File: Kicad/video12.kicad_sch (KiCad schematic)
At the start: 18 parts, among them J8001 DE15HD, U8001 THS7316, U8002 TPD7S019

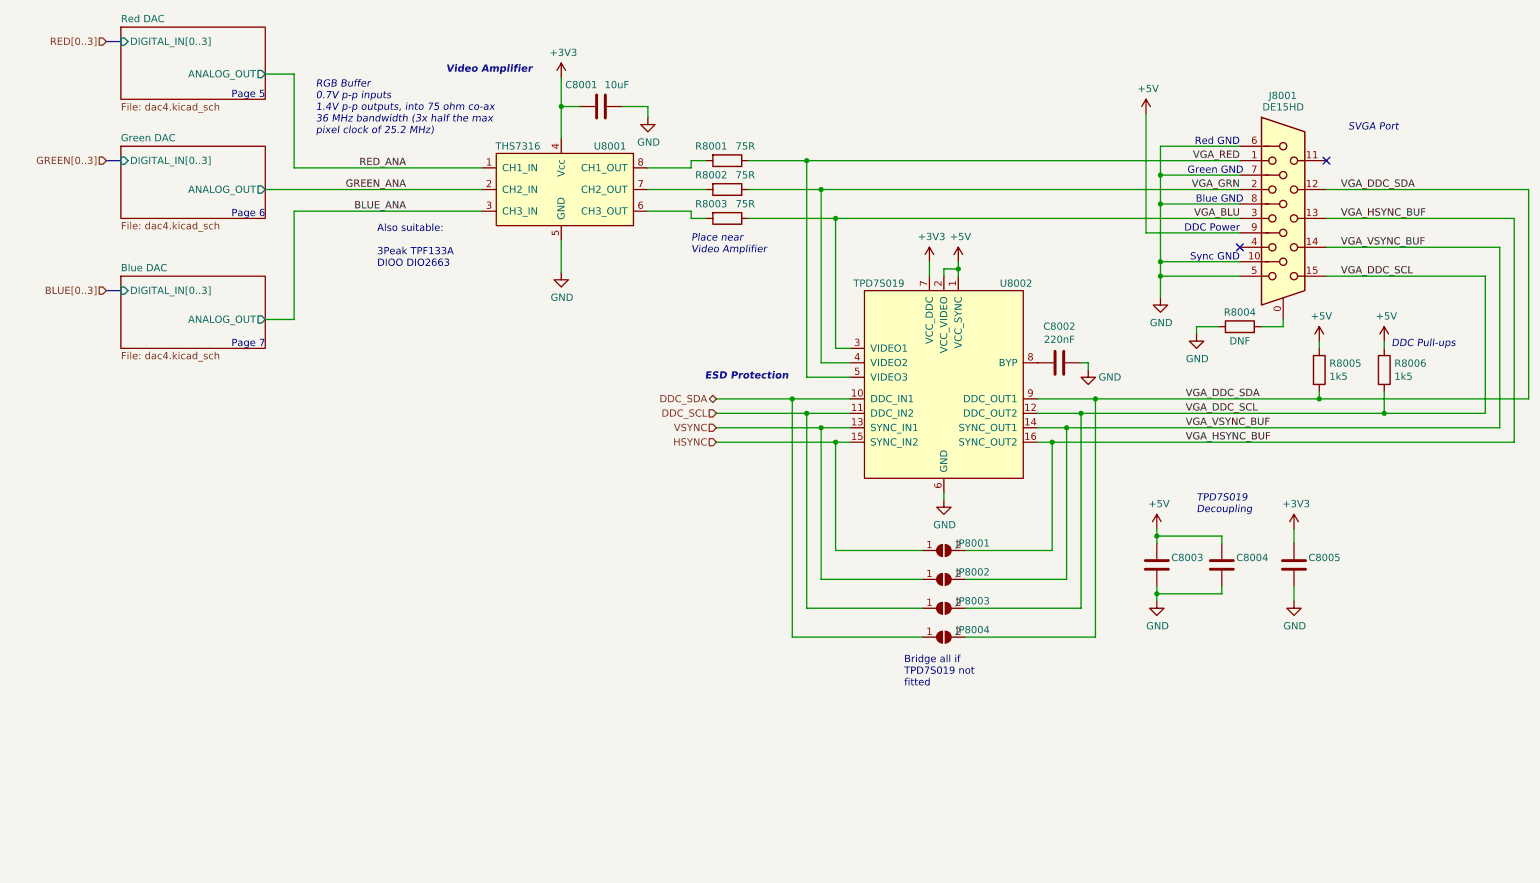
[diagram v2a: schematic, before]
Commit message: Set missing footprints and update PCB
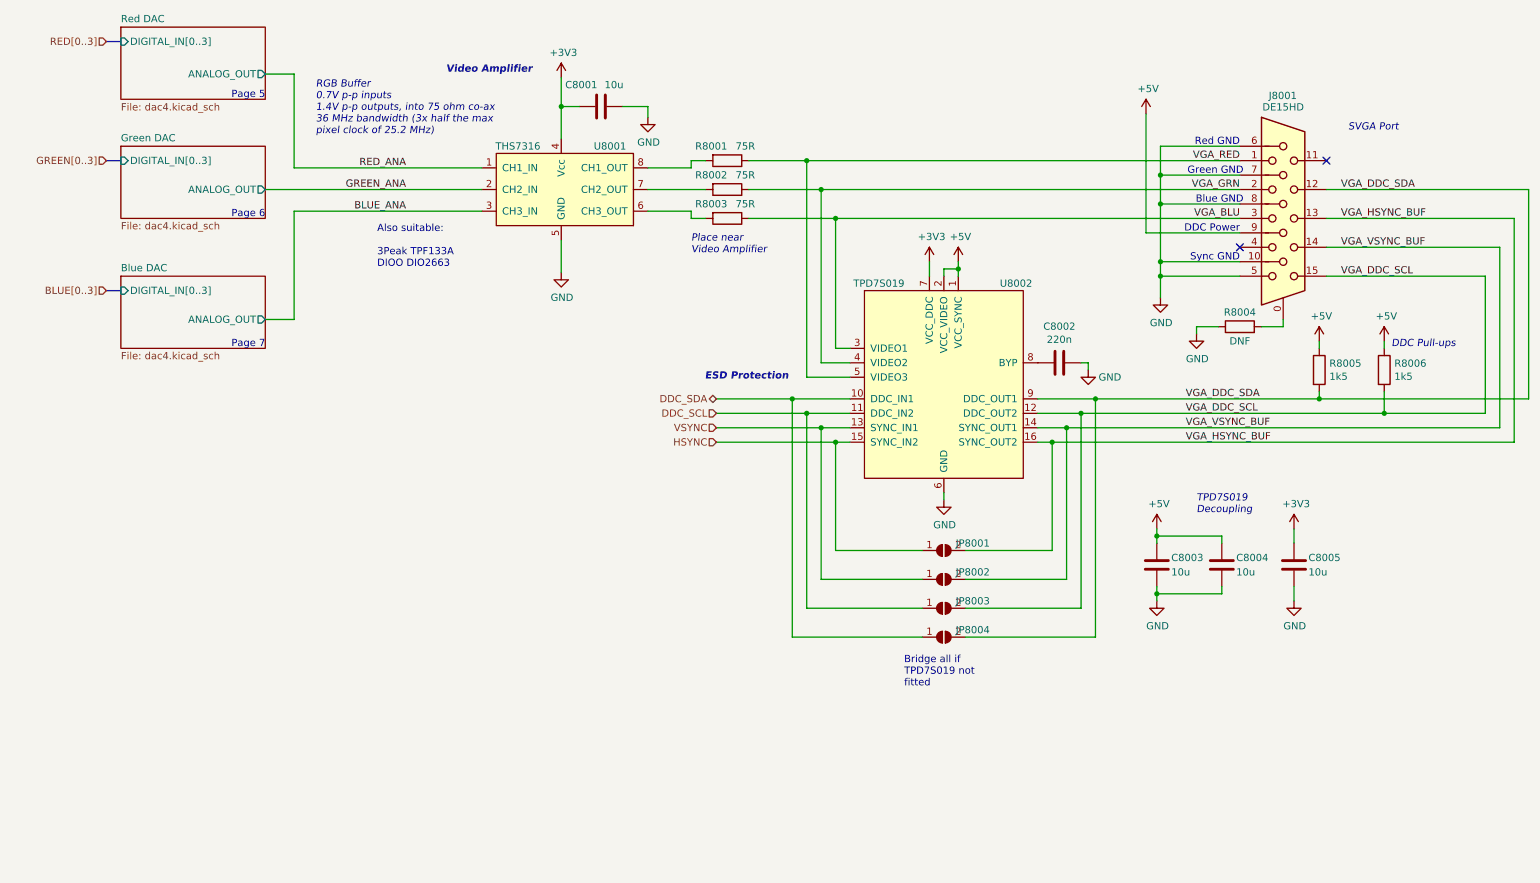
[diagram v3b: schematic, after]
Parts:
- C8001: value 10uF -> 10u; JLCPCB Collection Basic -> (none); LCSC Part# C15850 -> (none); MPN CL21A106KAYNNNE -> (none); Manufacturer Samsung -> (none)
- C8002: value 220nF -> 220n
- C8003, C8004, C8005: value (none) -> 10u; footprint (none) -> Capacitor_SMD:C_0805_2012Metric_Pad1.18x1.45mm_HandSolder; JLCPCB Collection Basic -> (none); LCSC Part# C15850 -> (none); MPN CL21A106KAYNNNE -> (none); Manufacturer Samsung -> (none)
- JP8001, JP8002, JP8003, JP8004: value (none) -> Bridge; footprint (none) -> Jumper:SolderJumper-2_P1.3mm_Open_RoundedPad1.0x1.5mm
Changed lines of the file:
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@@
       (effects (font (size 1.27 1.27)) (justify left))
     )
-    (property "Value" "10uF" (id 1) (at 118.11 55.245 90)
+    (property "Value" "10u" (id 1) (at 118.11 55.245 90)
       (effects (font (size 1.27 1.27)) (justify right))
     )
@@
       (effects (font (size 1.27 1.27)) hide)
     )
-    (property "Digikey" "~" (id 5) (at 117.475 59.055 0)
-      (effects (font (size 1.27 1.27)) hide)
-    )
-    (property "MPN" "CL21A106KAYNNNE" (id 6) (at 117.475 59.055 0)
-      (effects (font (size 1.27 1.27)) hide)
-    )
-    (property "Manufacturer" "Samsung" (id 7) (at 117.475 59.055 0)
-      (effects (font (size 1.27 1.27)) hide)
-    )
-    (property "LCSC Part#" "C15850" (id 8) (at 117.475 59.055 0)
+    (property "Digikey" "" (id 5) (at 117.475 59.055 0)
+      (effects (font (size 1.27 1.27)) hide)
+    )
+    (property "MPN" "" (id 6) (at 117.475 59.055 0)
+      (effects (font (size 1.27 1.27)) hide)
+    )
+    (property "Manufacturer" "" (id 7) (at 117.475 59.055 0)
+      (effects (font (size 1.27 1.27)) hide)
+    )
+    (property "LCSC Part#" "" (id 8) (at 117.475 59.055 0)
       (effects (font (size 1.27 1.27)) hide)
     )
@@
       (effects (font (size 1.27 1.27)) hide)
     )
-    (property "Mouser" "~" (id 11) (at 117.475 59.055 0)
-      (effects (font (size 1.27 1.27)) hide)
-    )
-    (property "JLCPCB Collection" "Basic" (id 12) (at 117.475 59.055 0)
+    (property "Mouser" "" (id 11) (at 117.475 59.055 0)
+      (effects (font (size 1.27 1.27)) hide)
+    )
+    (property "JLCPCB Collection" "" (id 12) (at 117.475 59.055 0)
       (effects (font (size 1.27 1.27)) hide)
     )
@@
     (in_bom yes) (on_board yes)
     (property "Reference" "C8002" (id 0) (at 198.12 97.7392 90))
-    (property "Value" "220nF" (id 1) (at 198.12 100.0506 90))
+    (property "Value" "220n" (id 1) (at 198.12 100.0506 90))
     (property "Footprint" "Capacitor_SMD:C_0805_2012Metric_Pad1.18x1.45mm_HandSolder" (id 2) (at 194.31 105.1052 0)
       (effects (font (size 1.27 1.27)) hide)
@@
       (effects (font (size 1.27 1.27)) (justify left))
     )
-    (property "Value" "" (id 1) (at 217.805 140.97 0)
-      (effects (font (size 1.27 1.27)) (justify left))
-    )
-    (property "Footprint" "" (id 2) (at 216.2302 135.89 0)
+    (property "Value" "10u" (id 1) (at 217.805 140.97 0)
+      (effects (font (size 1.27 1.27)) (justify left))
+    )
+    (property "Footprint" "Capacitor_SMD:C_0805_2012Metric_Pad1.18x1.45mm_HandSolder" (id 2) (at 216.2302 135.89 0)
       (effects (font (size 1.27 1.27)) hide)
     )
@@
       (effects (font (size 1.27 1.27)) hide)
     )
-    (property "Digikey" "~" (id 5) (at 215.265 139.7 0)
-      (effects (font (size 1.27 1.27)) hide)
-    )
-    (property "MPN" "CL21A106KAYNNNE" (id 6) (at 215.265 139.7 0)
-      (effects (font (size 1.27 1.27)) hide)
-    )
-    (property "Manufacturer" "Samsung" (id 7) (at 215.265 139.7 0)
-      (effects (font (size 1.27 1.27)) hide)
-    )
-    (property "LCSC Part#" "C15850" (id 8) (at 215.265 139.7 0)
+    (property "Digikey" "" (id 5) (at 215.265 139.7 0)
+      (effects (font (size 1.27 1.27)) hide)
+    )
+    (property "MPN" "" (id 6) (at 215.265 139.7 0)
+      (effects (font (size 1.27 1.27)) hide)
+    )
+    (property "Manufacturer" "" (id 7) (at 215.265 139.7 0)
+      (effects (font (size 1.27 1.27)) hide)
+    )
+    (property "LCSC Part#" "" (id 8) (at 215.265 139.7 0)
       (effects (font (size 1.27 1.27)) hide)
     )
@@
       (effects (font (size 1.27 1.27)) hide)
     )
-    (property "Mouser" "~" (id 11) (at 215.265 139.7 0)
-      (effects (font (size 1.27 1.27)) hide)
-    )
-    (property "JLCPCB Collection" "Basic" (id 12) (at 215.265 139.7 0)
+    (property "Mouser" "" (id 11) (at 215.265 139.7 0)
+      (effects (font (size 1.27 1.27)) hide)
+    )
+    (property "JLCPCB Collection" "" (id 12) (at 215.265 139.7 0)
       (effects (font (size 1.27 1.27)) hide)
     )
@@
     (in_bom yes) (on_board yes)
     (property "Reference" "JP8002" (id 0) (at 182.88 140.97 0))
-    (property "Value" "" (id 1) (at 177.8 139.7 0)
-      (effects (font (size 1.27 1.27)) hide)
-    )
-    (property "Footprint" "" (id 2) (at 177.8 142.24 0)
+    (property "Value" "Bridge" (id 1) (at 177.8 139.7 0)
+      (effects (font (size 1.27 1.27)) hide)
+    )
+    (property "Footprint" "Jumper:SolderJumper-2_P1.3mm_Open_RoundedPad1.0x1.5mm" (id 2) (at 177.8 142.24 0)
       (effects (font (size 1.27 1.27)) hide)
     )
@@
       (effects (font (size 1.27 1.27)) (justify left))
     )
-    (property "Value" "" (id 1) (at 241.935 140.97 0)
-      (effects (font (size 1.27 1.27)) (justify left))
-    )
-    (property "Footprint" "" (id 2) (at 240.3602 135.89 0)
+    (property "Value" "10u" (id 1) (at 241.935 140.97 0)
+      (effects (font (size 1.27 1.27)) (justify left))
+    )
+    (property "Footprint" "Capacitor_SMD:C_0805_2012Metric_Pad1.18x1.45mm_HandSolder" (id 2) (at 240.3602 135.89 0)
       (effects (font (size 1.27 1.27)) hide)
     )
@@
       (effects (font (size 1.27 1.27)) hide)
     )
-    (property "Digikey" "~" (id 5) (at 239.395 139.7 0)
-      (effects (font (size 1.27 1.27)) hide)
-    )
-    (property "MPN" "CL21A106KAYNNNE" (id 6) (at 239.395 139.7 0)
-      (effects (font (size 1.27 1.27)) hide)
-    )
-    (property "Manufacturer" "Samsung" (id 7) (at 239.395 139.7 0)
-      (effects (font (size 1.27 1.27)) hide)
-    )
-    (property "LCSC Part#" "C15850" (id 8) (at 239.395 139.7 0)
+    (property "Digikey" "" (id 5) (at 239.395 139.7 0)
+      (effects (font (size 1.27 1.27)) hide)
+    )
+    (property "MPN" "" (id 6) (at 239.395 139.7 0)
+      (effects (font (size 1.27 1.27)) hide)
+    )
+    (property "Manufacturer" "" (id 7) (at 239.395 139.7 0)
+      (effects (font (size 1.27 1.27)) hide)
+    )
+    (property "LCSC Part#" "" (id 8) (at 239.395 139.7 0)
       (effects (font (size 1.27 1.27)) hide)
     )
@@
       (effects (font (size 1.27 1.27)) hide)
     )
-    (property "Mouser" "~" (id 11) (at 239.395 139.7 0)
-      (effects (font (size 1.27 1.27)) hide)
-    )
-    (property "JLCPCB Collection" "Basic" (id 12) (at 239.395 139.7 0)
+    (property "Mouser" "" (id 11) (at 239.395 139.7 0)
+      (effects (font (size 1.27 1.27)) hide)
+    )
+    (property "JLCPCB Collection" "" (id 12) (at 239.395 139.7 0)
       (effects (font (size 1.27 1.27)) hide)
     )
@@
     (in_bom yes) (on_board yes)
     (property "Reference" "JP8004" (id 0) (at 182.88 151.13 0))
-    (property "Value" "" (id 1) (at 177.8 149.86 0)
-      (effects (font (size 1.27 1.27)) hide)
-    )
-    (property "Footprint" "" (id 2) (at 177.8 152.4 0)
+    (property "Value" "Bridge" (id 1) (at 177.8 149.86 0)
+      (effects (font (size 1.27 1.27)) hide)
+    )
+    (property "Footprint" "Jumper:SolderJumper-2_P1.3mm_Open_RoundedPad1.0x1.5mm" (id 2) (at 177.8 152.4 0)
       (effects (font (size 1.27 1.27)) hide)
     )
@@
     (in_bom yes) (on_board yes)
     (property "Reference" "JP8003" (id 0) (at 182.88 146.05 0))
-    (property "Value" "" (id 1) (at 177.8 144.78 0)
-      (effects (font (size 1.27 1.27)) hide)
-    )
-    (property "Footprint" "" (id 2) (at 177.8 147.32 0)
+    (property "Value" "Bridge" (id 1) (at 177.8 144.78 0)
+      (effects (font (size 1.27 1.27)) hide)
+    )
+    (property "Footprint" "Jumper:SolderJumper-2_P1.3mm_Open_RoundedPad1.0x1.5mm" (id 2) (at 177.8 147.32 0)
       (effects (font (size 1.27 1.27)) hide)
     )
@@
       (effects (font (size 1.27 1.27)) (justify left))
     )
-    (property "Value" "" (id 1) (at 229.235 140.97 0)
-      (effects (font (size 1.27 1.27)) (justify left))
-    )
-    (property "Footprint" "" (id 2) (at 227.6602 135.89 0)
+    (property "Value" "10u" (id 1) (at 229.235 140.97 0)
+      (effects (font (size 1.27 1.27)) (justify left))
+    )
+    (property "Footprint" "Capacitor_SMD:C_0805_2012Metric_Pad1.18x1.45mm_HandSolder" (id 2) (at 227.6602 135.89 0)
       (effects (font (size 1.27 1.27)) hide)
     )
@@
       (effects (font (size 1.27 1.27)) hide)
     )
-    (property "Digikey" "~" (id 5) (at 226.695 139.7 0)
-      (effects (font (size 1.27 1.27)) hide)
-    )
-    (property "MPN" "CL21A106KAYNNNE" (id 6) (at 226.695 139.7 0)
-      (effects (font (size 1.27 1.27)) hide)
-    )
-    (property "Manufacturer" "Samsung" (id 7) (at 226.695 139.7 0)
-      (effects (font (size 1.27 1.27)) hide)
-    )
-    (property "LCSC Part#" "C15850" (id 8) (at 226.695 139.7 0)
+    (property "Digikey" "" (id 5) (at 226.695 139.7 0)
+      (effects (font (size 1.27 1.27)) hide)
+    )
+    (property "MPN" "" (id 6) (at 226.695 139.7 0)
+      (effects (font (size 1.27 1.27)) hide)
+    )
+    (property "Manufacturer" "" (id 7) (at 226.695 139.7 0)
+      (effects (font (size 1.27 1.27)) hide)
+    )
+    (property "LCSC Part#" "" (id 8) (at 226.695 139.7 0)
       (effects (font (size 1.27 1.27)) hide)
     )
@@
       (effects (font (size 1.27 1.27)) hide)
     )
-    (property "Mouser" "~" (id 11) (at 226.695 139.7 0)
-      (effects (font (size 1.27 1.27)) hide)
-    )
-    (property "JLCPCB Collection" "Basic" (id 12) (at 226.695 139.7 0)
+    (property "Mouser" "" (id 11) (at 226.695 139.7 0)
+      (effects (font (size 1.27 1.27)) hide)
+    )
+    (property "JLCPCB Collection" "" (id 12) (at 226.695 139.7 0)
       (effects (font (size 1.27 1.27)) hide)
     )
@@
     (in_bom yes) (on_board yes)
     (property "Reference" "JP8001" (id 0) (at 182.88 135.89 0))
-    (property "Value" "" (id 1) (at 177.8 134.62 0)
-      (effects (font (size 1.27 1.27)) hide)
-    )
-    (property "Footprint" "" (id 2) (at 177.8 137.16 0)
-      (effects (font (size 1.27 1.27)) hide)
-    )
+    (property "Value" "Bridge" (id 1) (at 177.8 134.62 0)
+      (effects (font (size 1.27 1.27)) hide)
+    )
+    (property "Footprint" "Jumper:SolderJumper-2_P1.3mm_Open_RoundedPad1.0x1.5mm" (id 2) (at 177.8 137.16 0)
+      (effects (font (size 1.27 1.27)) hide)
+    )

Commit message: Re-imported from Neotron Pico v1.1.
This time I deleted the sheets from the top level and then re-added pointing at the new files. I also reset the PCB dimensions to match the Neotron Pico.

This seems to have done a better job importing footprints.
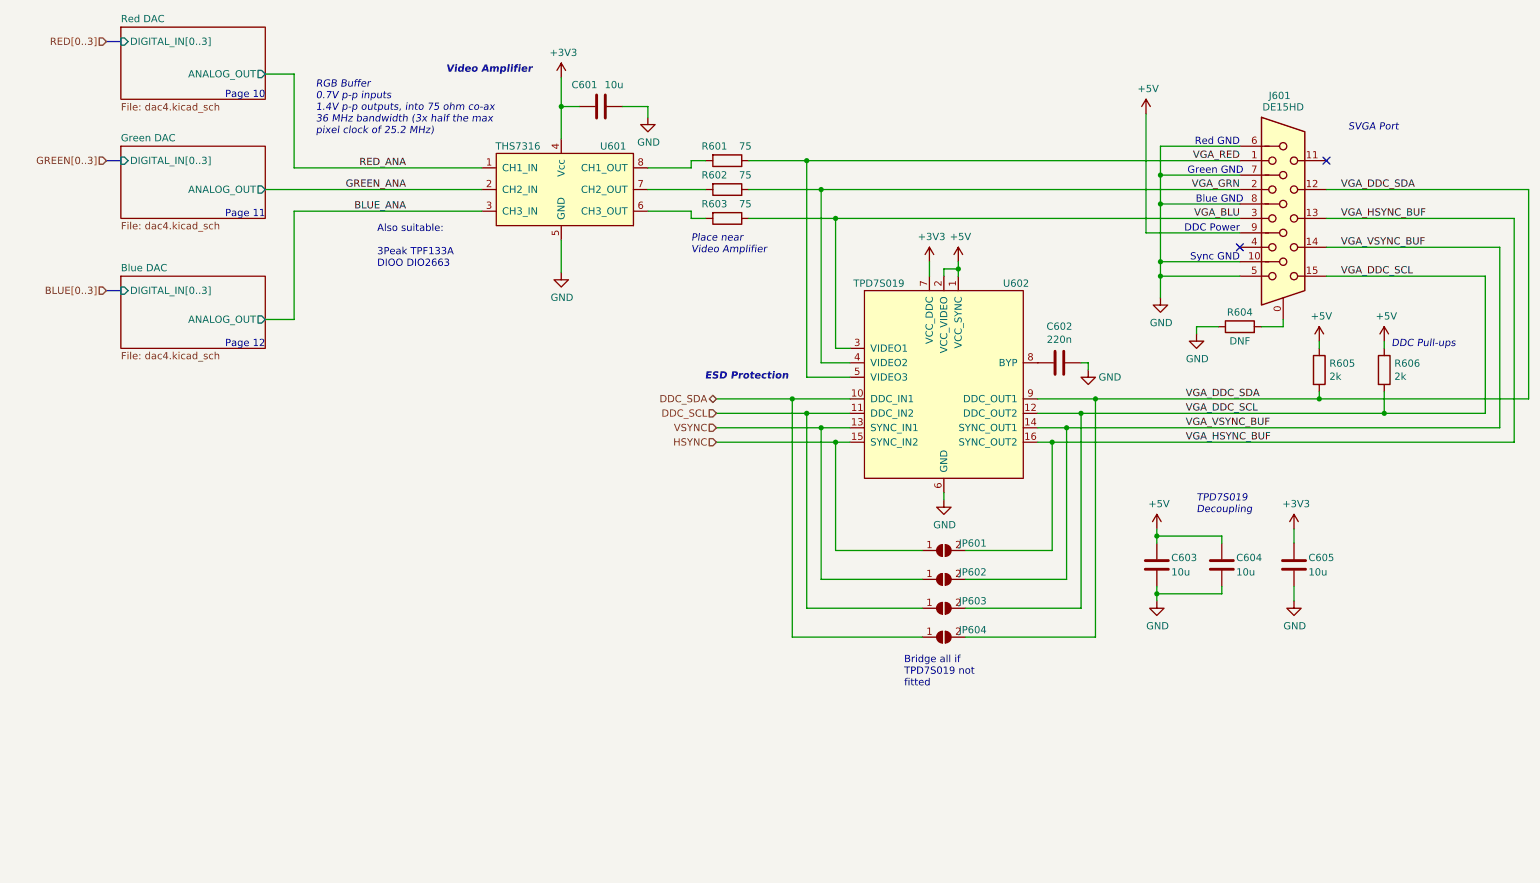
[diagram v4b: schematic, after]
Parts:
- C601: renamed from C8001; JLCPCB Collection (none) -> Basic; LCSC Part# (none) -> C15850; MPN (none) -> CL21A106KAYNNNE; Manufacturer (none) -> Samsung
- C603: renamed from C8003; JLCPCB Collection (none) -> Basic; LCSC Part# (none) -> C15850; MPN (none) -> CL21A106KAYNNNE; Manufacturer (none) -> Samsung
- C604: renamed from C8004; JLCPCB Collection (none) -> Basic; LCSC Part# (none) -> C15850; MPN (none) -> CL21A106KAYNNNE; Manufacturer (none) -> Samsung
- C605: renamed from C8005; JLCPCB Collection (none) -> Basic; LCSC Part# (none) -> C15850; MPN (none) -> CL21A106KAYNNNE; Manufacturer (none) -> Samsung
- R601: renamed from R8001; value 75R -> 75
- R602: renamed from R8002; value 75R -> 75
- R603: renamed from R8003; value 75R -> 75
- R605: renamed from R8005; value 1k5 -> 2k
- R606: renamed from R8006; value 1k5 -> 2k
- renumbered C8002 to C602, J8001 to J601, JP8001 to JP601, JP8002 to JP602, JP8003 to JP603, JP8004 to JP604, R8004 to R604, U8001 to U601, U8002 to U602
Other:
- note added: "Page 10"
- note added: "Page 11"
- note added: "Page 12"
- note removed: "Page 5"
- note removed: "Page 6"
- note removed: "Page 7"
- company: https://neotron-compute.github.io -> https://neotron-compute.github.io/
